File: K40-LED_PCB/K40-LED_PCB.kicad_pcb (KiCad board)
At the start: 2 copper layers, 26.5 x 61.5 mm, 29 parts, among them U1 LDD_350HS, U2 LM3466, U3 LM3466, U4 LM3466, U5 LM3466, p1 12V_Pad

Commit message: Cont Traces
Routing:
- net Net-(C1-Pad1): track 0.00 -> 125.4 mm
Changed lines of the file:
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@@
     (thickness 1.6)
     (drawings 3)
-    (tracks 26)
+    (tracks 38)
     (zones 0)
     (modules 29)
@@
   (segment (start 158.4 98.8125) (end 158.4 108.97) (width 0.25) (layer F.Cu) (net 5))
   (segment (start 134 134.4) (end 134 136.94) (width 0.25) (layer F.Cu) (net 6))
+  (segment (start 90.9612 106.2482) (end 106.2482 106.2482) (width 0.25) (layer F.Cu) (net 7))
+  (segment (start 107 107) (end 107 122) (width 0.25) (layer F.Cu) (net 7))
+  (segment (start 106.2482 106.2482) (end 107 107) (width 0.25) (layer F.Cu) (net 7))
+  (segment (start 75.1482 122.2388) (end 75.1482 106.9518) (width 0.25) (layer F.Cu) (net 7))
+  (segment (start 75.1482 106.9518) (end 75.9 106.2) (width 0.25) (layer F.Cu) (net 7))
+  (segment (start 75.9 106.2) (end 90.9 106.2) (width 0.25) (layer F.Cu) (net 7))
+  (segment (start 75.2 137.4) (end 75.2 122.4) (width 0.25) (layer F.Cu) (net 7))
+  (segment (start 75.9518 138.1518) (end 75.2 137.4) (width 0.25) (layer F.Cu) (net 7))
+  (segment (start 91.2388 138.1518) (end 75.9518 138.1518) (width 0.25) (layer F.Cu) (net 7))
+  (segment (start 106.9518 122.0612) (end 106.9518 137.3482) (width 0.25) (layer F.Cu) (net 7))
+  (segment (start 106.9518 137.3482) (end 106.2 138.1) (width 0.25) (layer F.Cu) (net 7))
+  (segment (start 106.2 138.1) (end 91.2 138.1) (width 0.25) (layer F.Cu) (net 7))
   (segment (start 158.3875 97) (end 158.4 96.9875) (width 0.25) (layer F.Cu) (net 13))
   (segment (start 150.5 97) (end 158.3875 97) (width 0.25) (layer F.Cu) (net 13))

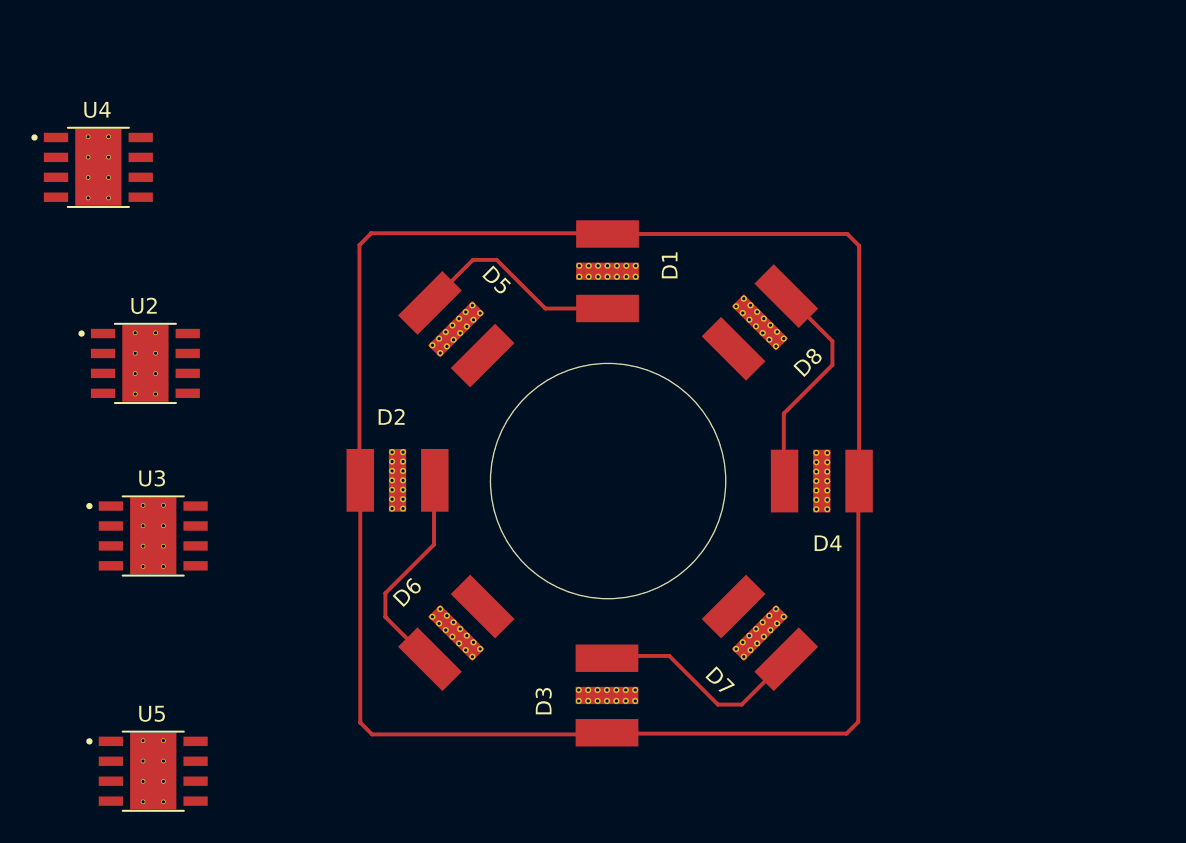
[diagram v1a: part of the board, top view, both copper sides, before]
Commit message: More_PCB Updates LM3466 movementr
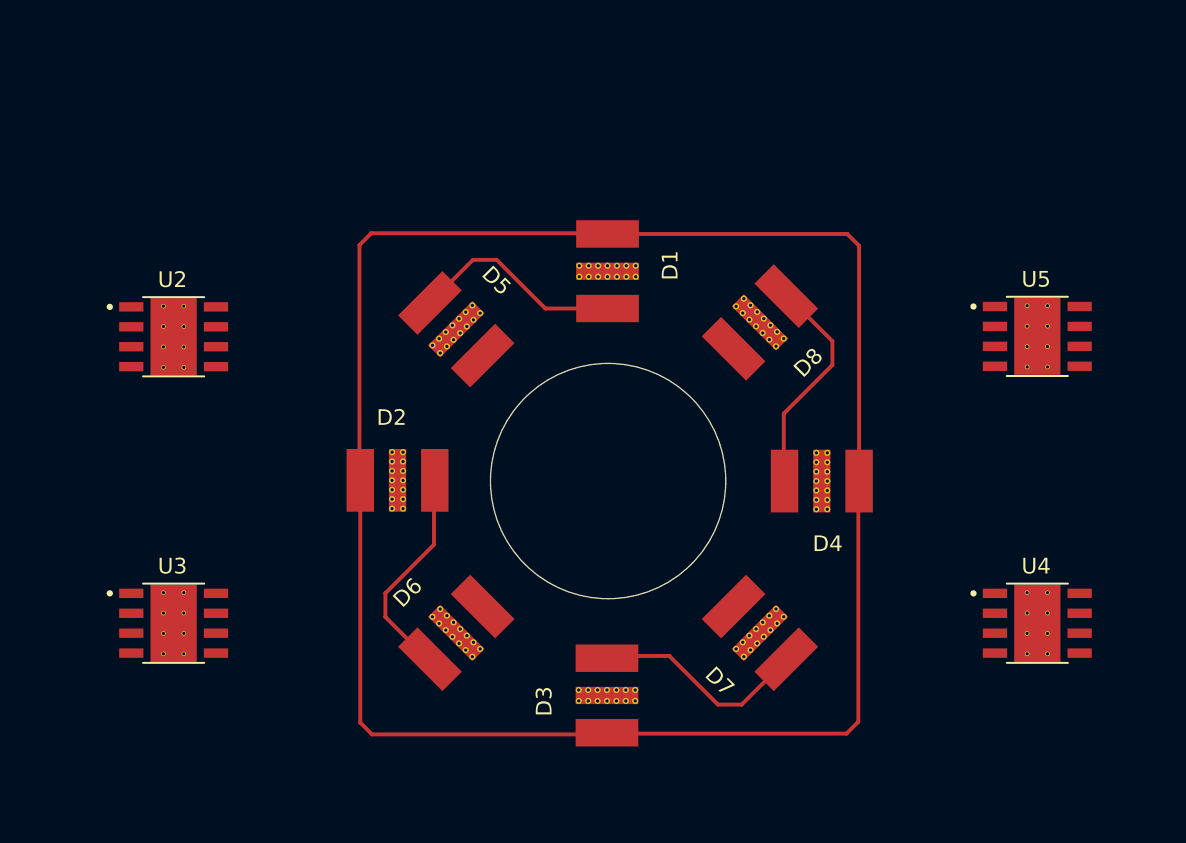
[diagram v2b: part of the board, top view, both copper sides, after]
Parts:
- moved U4 66.5 mm to (118.4, 131.1)
- moved U5 62.8 mm to (118.4, 112.8)
- moved U3 5.71 mm to (63.3, 131.1)
- moved U2 2.48 mm to (63.3, 112.8)

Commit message: More PCB Updates
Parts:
- moved R2 95.4 mm to (71.0, 115.7), turned to 90 degrees
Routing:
- net Net-(C2-Pad1): track 0.00 -> 27.7 mm, vias 0 -> 2
- net Net-(C8-Pad1): track 0.00 -> 25.6 mm, vias 0 -> 2
- net Net-(C6-Pad1): track 0.00 -> 19.0 mm, vias 0 -> 2
- net Net-(R2-Pad2): track 0.00 -> 18.9 mm
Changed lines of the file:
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@@
     (thickness 1.6)
     (drawings 3)
-    (tracks 38)
+    (tracks 75)
     (zones 0)
     (modules 29)
@@
   )
   (module Resistor_SMD:R_0805_2012Metric (layer F.Cu)
-    (at 158.2 76.98)
+    (at 71 115.6875 90)
     (descr "Resistor SMD 0805 (2012 Metric), square (rectangular) end terminal, IPC_7351 nominal, (Body size source: IPC-SM-782 page 72, https://www.pcb-3d.com/wordpress/wp-content/uploads/ipc-sm-782a_amendment_1_and_2.pdf), generated with kicad-footprint-generator")
     (tags resistor)
     (attr smd)
-    (fp_text reference R2 (at 0 -1.65) (layer F.SilkS)
-      (effects (font (size 1 1) (thickness 0.15)))
-    )
-    (fp_text value 1 (at 0 1.65) (layer F.Fab)
-      (effects (font (size 1 1) (thickness 0.15)))
-    )
-    (fp_text user %R (at 0 0) (layer F.Fab)
+    (fp_text reference R2 (at 0 -1.65 90) (layer F.SilkS)
+      (effects (font (size 1 1) (thickness 0.15)))
+    )
+    (fp_text value 1 (at 0 1.65 90) (layer F.Fab)
+      (effects (font (size 1 1) (thickness 0.15)))
+    )
+    (fp_text user %R (at 0 0 90) (layer F.Fab)
       (effects (font (size 0.5 0.5) (thickness 0.08)))
     )
@@
     (fp_line (start 1.68 -0.95) (end 1.68 0.95) (layer F.CrtYd) (width 0.05))
     (fp_line (start 1.68 0.95) (end -1.68 0.95) (layer F.CrtYd) (width 0.05))
-    (pad 2 smd roundrect (at 0.9125 0) (size 1.025 1.4) (layers F.Cu F.Paste F.Mask) (roundrect_rratio 0.243902)
+    (pad 2 smd roundrect (at 0.9125 0 90) (size 1.025 1.4) (layers F.Cu F.Paste F.Mask) (roundrect_rratio 0.243902)
       (net 14 "Net-(R2-Pad2)"))
-    (pad 1 smd roundrect (at -0.9125 0) (size 1.025 1.4) (layers F.Cu F.Paste F.Mask) (roundrect_rratio 0.243902)
+    (pad 1 smd roundrect (at -0.9125 0 90) (size 1.025 1.4) (layers F.Cu F.Paste F.Mask) (roundrect_rratio 0.243902)
       (net 6 GND))
     (model ${KISYS3DMOD}/Resistor_SMD.3dshapes/R_0805_2012Metric.wrl
@@
   (segment (start 102.258757 133.508757) (end 99.517514 136.25) (width 0.25) (layer F.Cu) (net 3))
   (segment (start 98 136.25) (end 94.9 133.15) (width 0.25) (layer F.Cu) (net 3))
-  (segment (start 158.37 109) (end 158.37 111.54) (width 0.25) (layer F.Cu) (net 5))
   (segment (start 158.4 108.97) (end 158.37 109) (width 0.25) (layer F.Cu) (net 5))
-  (segment (start 158.4 98.8125) (end 158.4 108.97) (width 0.25) (layer F.Cu) (net 5))
-  (segment (start 134 134.4) (end 134 136.94) (width 0.25) (layer F.Cu) (net 6))
-  (segment (start 90.9612 106.2482) (end 106.2482 106.2482) (width 0.25) (layer F.Cu) (net 7))
-  (segment (start 107 107) (end 107 122) (width 0.25) (layer F.Cu) (net 7))
-  (segment (start 106.2482 106.2482) (end 107 107) (width 0.25) (layer F.Cu) (net 7))
-  (segment (start 75.1482 122.2388) (end 75.1482 106.9518) (width 0.25) (layer F.Cu) (net 7))
-  (segment (start 75.1482 106.9518) (end 75.9 106.2) (width 0.25) (layer F.Cu) (net 7))
-  (segment (start 75.9 106.2) (end 90.9 106.2) (width 0.25) (layer F.Cu) (net 7))
-  (segment (start 75.2 137.4) (end 75.2 122.4) (width 0.25) (layer F.Cu) (net 7))
-  (segment (start 75.9518 138.1518) (end 75.2 137.4) (width 0.25) (layer F.Cu) (net 7))
-  (segment (start 91.2388 138.1518) (end 75.9518 138.1518) (width 0.25) (layer F.Cu) (net 7))
-  (segment (start 106.9518 122.0612) (end 106.9518 137.3482) (width 0.25) (layer F.Cu) (net 7))
-  (segment (start 106.9518 137.3482) (end 106.2 138.1) (width 0.25) (layer F.Cu) (net 7))
-  (segment (start 106.2 138.1) (end 91.2 138.1) (width 0.25) (layer F.Cu) (net 7))
+  (segment (start 158.4 98.8125) (end 158.4 108.97) (width 0.381) (layer F.Cu) (net 5))
+  (segment (start 158.37 109) (end 158.37 111.54) (width 0.381) (layer F.Cu) (net 5))
+  (segment (start 134 134.4) (end 134 136.94) (width 0.381) (layer F.Cu) (net 6))
+  (segment (start 90.9612 106.2482) (end 106.2482 106.2482) (width 0.381) (layer F.Cu) (net 7))
+  (segment (start 107 107) (end 107 122) (width 0.381) (layer F.Cu) (net 7))
+  (segment (start 106.2482 106.2482) (end 107 107) (width 0.381) (layer F.Cu) (net 7))
+  (segment (start 75.1482 122.2388) (end 75.1482 106.9518) (width 0.381) (layer F.Cu) (net 7))
+  (segment (start 75.1482 106.9518) (end 75.9 106.2) (width 0.381) (layer F.Cu) (net 7))
+  (segment (start 75.9 106.2) (end 90.9 106.2) (width 0.381) (layer F.Cu) (net 7))
+  (segment (start 75.2 137.4) (end 75.2 122.4) (width 0.381) (layer F.Cu) (net 7))
+  (segment (start 75.9518 138.1518) (end 75.2 137.4) (width 0.381) (layer F.Cu) (net 7))
+  (segment (start 91.2388 138.1518) (end 75.9518 138.1518) (width 0.381) (layer F.Cu) (net 7))
+  (segment (start 106.9518 122.0612) (end 106.9518 137.3482) (width 0.381) (layer F.Cu) (net 7))
+  (segment (start 106.9518 137.3482) (end 106.2 138.1) (width 0.381) (layer F.Cu) (net 7))
+  (segment (start 106.2 138.1) (end 91.2 138.1) (width 0.381) (layer F.Cu) (net 7))
+  (segment (start 83 114) (end 80.6 116.4) (width 0.25) (layer F.Cu) (net 8))
+  (segment (start 80.6 116.4) (end 80.2 116.4) (width 0.25) (layer F.Cu) (net 8))
+  (via (at 76.2 112.6) (size 0.8) (drill 0.4) (layers F.Cu B.Cu) (net 8))
+  (segment (start 80 116.4) (end 76.2 112.6) (width 0.25) (layer F.Cu) (net 8))
+  (segment (start 80.2 116.4) (end 80 116.4) (width 0.25) (layer F.Cu) (net 8))
+  (via (at 74.2 110.6) (size 0.8) (drill 0.4) (layers F.Cu B.Cu) (net 8))
+  (segment (start 76.2 112.6) (end 74.2 110.6) (width 0.25) (layer B.Cu) (net 8))
+  (segment (start 74.2 110.6) (end 73 109.4) (width 0.25) (layer F.Cu) (net 8))
+  (segment (start 73 109.4) (end 60.8 109.4) (width 0.25) (layer F.Cu) (net 8))
+  (segment (start 60.6 109.6) (end 60.6 110.895) (width 0.25) (layer F.Cu) (net 8))
+  (segment (start 60.8 109.4) (end 60.6 109.6) (width 0.25) (layer F.Cu) (net 8))
+  (via (at 108 126.8) (size 0.8) (drill 0.4) (layers F.Cu B.Cu) (net 10))
+  (segment (start 110.359 129.159) (end 108 126.8) (width 0.25) (layer F.Cu) (net 10))
+  (segment (start 115.664 129.159) (end 110.359 129.159) (width 0.25) (layer F.Cu) (net 10))
+  (via (at 106 126.8) (size 0.8) (drill 0.4) (layers F.Cu B.Cu) (net 10))
+  (segment (start 108 126.8) (end 106 126.8) (width 0.25) (layer B.Cu) (net 10))
+  (segment (start 102.2 126.8) (end 99 130) (width 0.25) (layer F.Cu) (net 10))
+  (segment (start 106 126.8) (end 102.2 126.8) (width 0.25) (layer F.Cu) (net 10))
+  (segment (start 115.664 110.871) (end 109.855 110.871) (width 0.25) (layer F.Cu) (net 11))
+  (via (at 107.95 108.966) (size 0.8) (drill 0.4) (layers F.Cu B.Cu) (net 11))
+  (segment (start 109.855 110.871) (end 107.95 108.966) (width 0.25) (layer F.Cu) (net 11))
+  (via (at 105.6 107.2) (size 0.8) (drill 0.4) (layers F.Cu B.Cu) (net 11))
+  (segment (start 100.407357 107.2) (end 105.6 107.2) (width 0.25) (layer F.Cu) (net 11))
+  (segment (start 106.184 107.2) (end 107.95 108.966) (width 0.25) (layer B.Cu) (net 11))
+  (segment (start 105.6 107.2) (end 106.184 107.2) (width 0.25) (layer B.Cu) (net 11))
+  (segment (start 96.703679 111.271036) (end 96.703679 110.903679) (width 0.25) (layer F.Cu) (net 11))
+  (segment (start 99 113.567357) (end 96.703679 111.271036) (width 0.25) (layer F.Cu) (net 11))
+  (segment (start 96.703679 110.903679) (end 100.407357 107.2) (width 0.25) (layer F.Cu) (net 11))
   (segment (start 158.3875 97) (end 158.4 96.9875) (width 0.25) (layer F.Cu) (net 13))
-  (segment (start 150.5 97) (end 158.3875 97) (width 0.25) (layer F.Cu) (net 13))
-  (segment (start 134 109) (end 134 97.5) (width 0.25) (layer F.Cu) (net 24))
-  (segment (start 134.5 97) (end 142.5 97) (width 0.25) (layer F.Cu) (net 24))
-  (segment (start 134 97.5) (end 134.5 97) (width 0.25) (layer F.Cu) (net 24))
-  (segment (start 134 111.54) (end 134 109) (width 0.25) (layer F.Cu) (net 24))
+  (segment (start 150.5 97) (end 158.3875 97) (width 0.381) (layer F.Cu) (net 13))
+  (segment (start 66 110.895) (end 70.695 110.895) (width 0.25) (layer F.Cu) (net 14))
+  (segment (start 70.695 110.895) (end 71 111.2) (width 0.25) (layer F.Cu) (net 14))
+  (segment (start 70.765 112.165) (end 71 112.4) (width 0.25) (layer F.Cu) (net 14))
+  (segment (start 66 112.165) (end 70.765 112.165) (width 0.25) (layer F.Cu) (net 14))
+  (segment (start 71 111.2) (end 71 112.4) (width 0.25) (layer F.Cu) (net 14))
+  (segment (start 70.835 113.435) (end 71 113.6) (width 0.25) (layer F.Cu) (net 14))
+  (segment (start 66 113.435) (end 70.835 113.435) (width 0.25) (layer F.Cu) (net 14))
+  (segment (start 71 113.6) (end 71 114.775) (width 0.25) (layer F.Cu) (net 14))
+  (segment (start 71 112.4) (end 71 113.6) (width 0.25) (layer F.Cu) (net 14))
+  (segment (start 134 109) (end 134 97.5) (width 0.381) (layer F.Cu) (net 24))
+  (segment (start 134.5 97) (end 142.5 97) (width 0.381) (layer F.Cu) (net 24))
+  (segment (start 134 97.5) (end 134.5 97) (width 0.381) (layer F.Cu) (net 24))
+  (segment (start 134 111.54) (end 134 109) (width 0.381) (layer F.Cu) (net 24))
 )

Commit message: Updated more PCB
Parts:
- moved R3 124.4 mm to (71.0, 134.0), turned to 90 degrees
- moved R4 72.2 mm to (126.2, 133.8), turned to 90 degrees
- moved R5 63.4 mm to (126.2, 115.6), turned to 90 degrees
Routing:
- net GND: track 2.54 -> 25.9 mm
- net Net-(R5-Pad2): track 0.00 -> 18.9 mm
- net Net-(R4-Pad2): track 0.00 -> 18.9 mm
- net Net-(R3-Pad2): track 0.00 -> 18.9 mm

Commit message: Updated PCB  Again
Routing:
- net GND: track 25.9 -> 166.7 mm
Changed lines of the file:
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@@
     (thickness 1.6)
     (drawings 3)
-    (tracks 114)
+    (tracks 136)
     (zones 0)
     (modules 29)
@@
   (segment (start 69.9125 134.9125) (end 71 134.9125) (width 0.381) (layer F.Cu) (net 6))
   (segment (start 67.969 132.969) (end 69.9125 134.9125) (width 0.381) (layer F.Cu) (net 6))
-  (segment (start 121.064 114.681) (end 123.081 114.681) (width 0.25) (layer F.Cu) (net 6))
-  (segment (start 124.9125 116.5125) (end 126.2 116.5125) (width 0.25) (layer F.Cu) (net 6))
-  (segment (start 123.081 114.681) (end 124.9125 116.5125) (width 0.25) (layer F.Cu) (net 6))
-  (segment (start 121.064 132.969) (end 123.169 132.969) (width 0.25) (layer F.Cu) (net 6))
-  (segment (start 124.9125 134.7125) (end 126.2 134.7125) (width 0.25) (layer F.Cu) (net 6))
-  (segment (start 123.169 132.969) (end 124.9125 134.7125) (width 0.25) (layer F.Cu) (net 6))
+  (segment (start 121.064 114.681) (end 123.081 114.681) (width 0.381) (layer F.Cu) (net 6))
+  (segment (start 124.9125 116.5125) (end 126.2 116.5125) (width 0.381) (layer F.Cu) (net 6))
+  (segment (start 123.081 114.681) (end 124.9125 116.5125) (width 0.381) (layer F.Cu) (net 6))
+  (segment (start 121.064 132.969) (end 123.169 132.969) (width 0.381) (layer F.Cu) (net 6))
+  (segment (start 124.9125 134.7125) (end 126.2 134.7125) (width 0.381) (layer F.Cu) (net 6))
+  (segment (start 123.169 132.969) (end 124.9125 134.7125) (width 0.381) (layer F.Cu) (net 6))
+  (segment (start 66 114.705) (end 66 115.6) (width 0.381) (layer F.Cu) (net 6))
+  (segment (start 66 115.6) (end 73 122.6) (width 0.381) (layer F.Cu) (net 6))
+  (segment (start 66 132.969) (end 66 133.8) (width 0.381) (layer F.Cu) (net 6))
+  (segment (start 66 133.8) (end 71.2 139) (width 0.381) (layer F.Cu) (net 6))
+  (segment (start 73 138.6) (end 73.4 139) (width 0.381) (layer F.Cu) (net 6))
+  (segment (start 73 122.6) (end 73 138.6) (width 0.381) (layer F.Cu) (net 6))
+  (segment (start 71.2 139) (end 73.4 141.2) (width 0.381) (layer F.Cu) (net 6))
+  (segment (start 121.064 132.969) (end 121.064 133.936) (width 0.381) (layer F.Cu) (net 6))
+  (segment (start 121.064 133.936) (end 113.8 141.2) (width 0.381) (layer F.Cu) (net 6))
+  (segment (start 113.8 141.2) (end 113.6 141.2) (width 0.381) (layer F.Cu) (net 6))
+  (segment (start 73.4 139) (end 75.6 141.2) (width 0.381) (layer F.Cu) (net 6))
+  (segment (start 75.6 141.2) (end 73.4 141.2) (width 0.381) (layer F.Cu) (net 6))
+  (segment (start 113.6 141.2) (end 75.6 141.2) (width 0.381) (layer F.Cu) (net 6))
+  (segment (start 121.064 115.664) (end 128 122.6) (width 0.381) (layer F.Cu) (net 6))
+  (segment (start 121.064 114.681) (end 121.064 115.664) (width 0.381) (layer F.Cu) (net 6))
+  (segment (start 113.8 141.2) (end 115.6 141.2) (width 0.381) (layer F.Cu) (net 6))
+  (segment (start 115.6 141.2) (end 119.86 136.94) (width 0.381) (layer F.Cu) (net 6))
+  (segment (start 128 136.2) (end 128.74 136.94) (width 0.381) (layer F.Cu) (net 6))
+  (segment (start 128.74 136.94) (end 134 136.94) (width 0.381) (layer F.Cu) (net 6))
+  (segment (start 119.86 136.94) (end 128.74 136.94) (width 0.381) (layer F.Cu) (net 6))
+  (segment (start 128 122.6) (end 128 136) (width 0.381) (layer F.Cu) (net 6))
+  (segment (start 128 136.2) (end 128 136) (width 0.381) (layer F.Cu) (net 6))
   (segment (start 90.9612 106.2482) (end 106.2482 106.2482) (width 0.381) (layer F.Cu) (net 7))
   (segment (start 107 107) (end 107 122) (width 0.381) (layer F.Cu) (net 7))
